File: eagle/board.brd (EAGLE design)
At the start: 75 x 50 mm, 24 parts, among them X1 2.1MMJACKTHM, X10 10p-2.0, X11 MOUNTING_HOLE3.2MM_SILK, X12 MOUNTING_HOLE3.2MM_SILK, X13 MOUNTING_HOLE3.2MM_SILK, X14 MOUNTING_HOLE3.2MM_SILK, X2 2p-2.0, X3 5p-2.54, X4 8p-2.54, X5 14p-2.54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

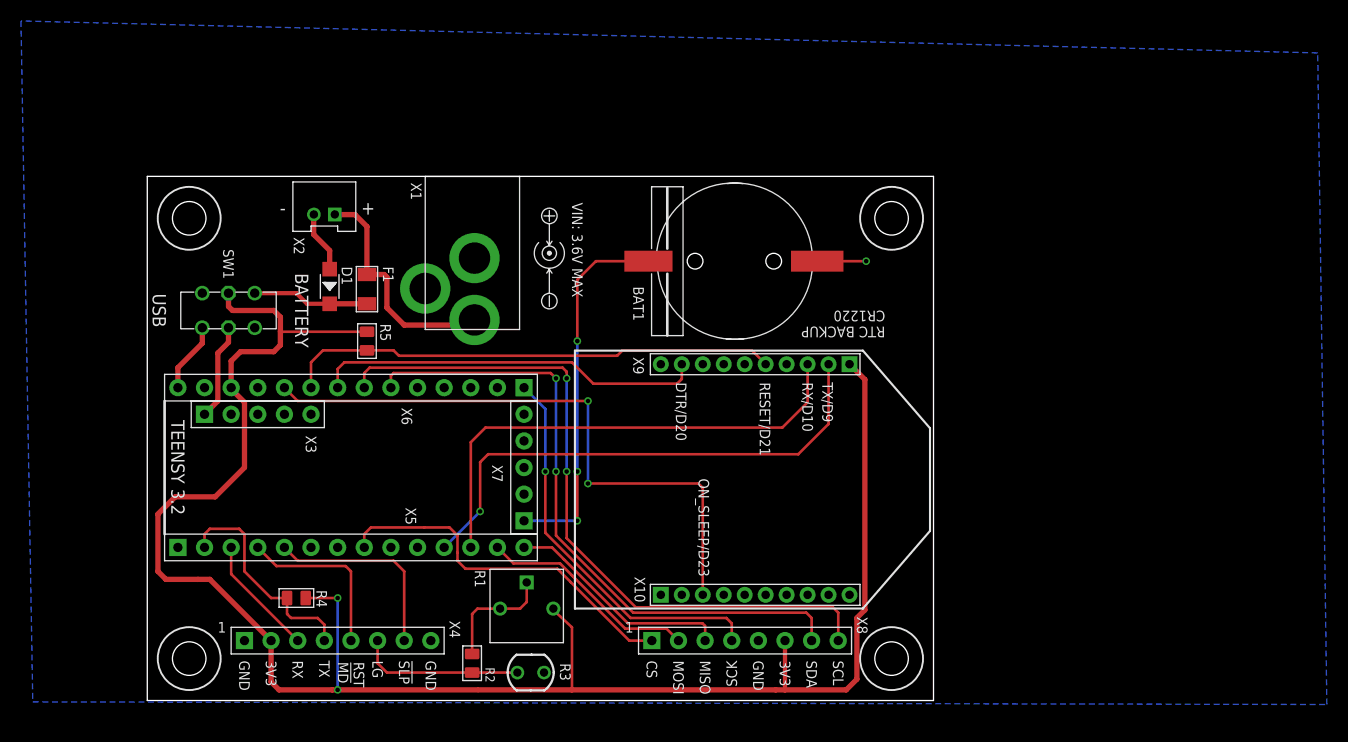
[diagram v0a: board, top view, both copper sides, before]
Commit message: new slide switch new capacitors
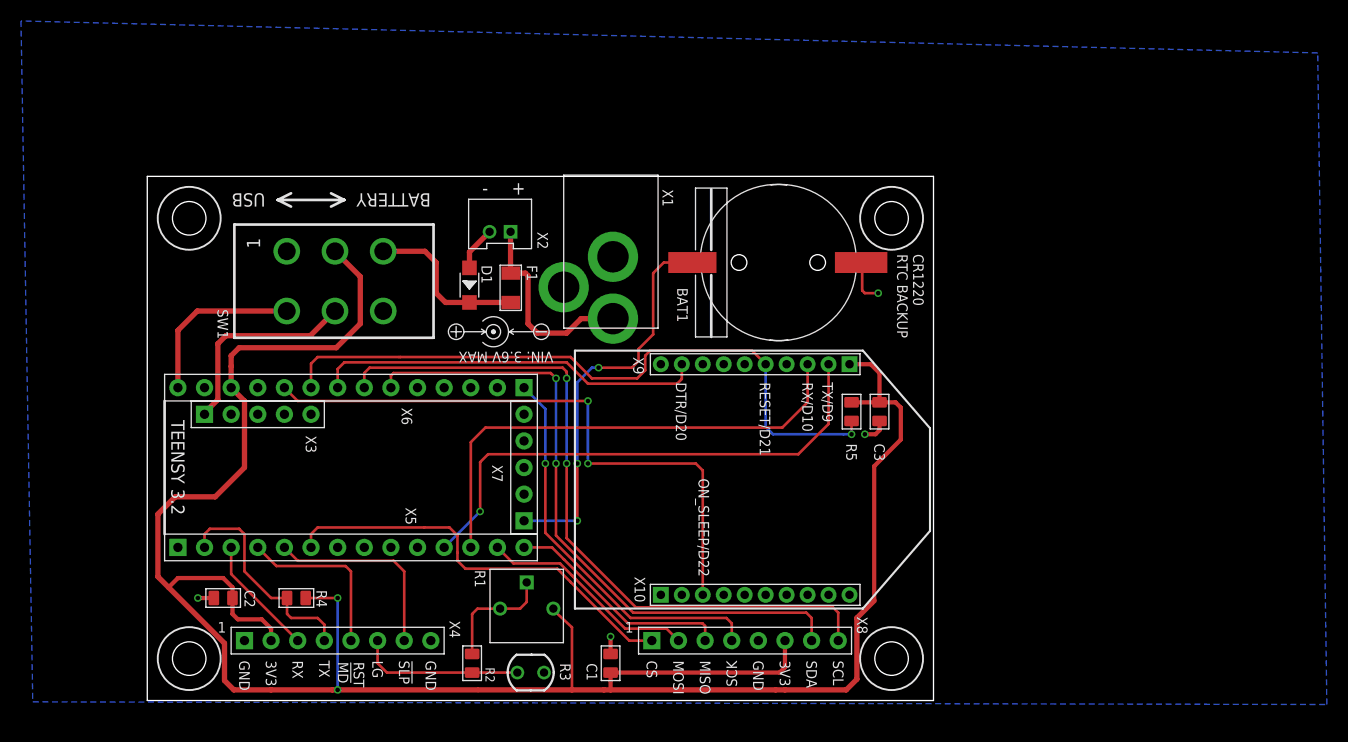
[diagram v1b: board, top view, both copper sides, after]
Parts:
- added C1, C2, C3: 2.2uf, Seeed-OPL-Capacitor:C0805
- SW1: value (none) -> C&K L202XXYYXMS; device teensybee:SW6-2.54-9.0X3.5X3.2+2.0MM -> teensybee:C&K_L102_MS
- moved R5 46.7 mm to (67.2, 27.6)
- moved X2 16.8 mm to (33.7, 45.5)
- moved F1 13.7 mm to (34.7, 39.4)
- moved D1 13.3 mm to (30.7, 39.6)
- moved X1 13.2 mm to (44.3, 45.7)
- moved SW1 10.5 mm to (17.9, 40.0), turned to 270 degrees
- moved U$1 9.20 mm to (33.0, 35.2), turned to 0 degrees
- moved BAT1 4.19 mm to (60.2, 41.8)
- renumbered X11 to MNT1, X12 to MNT2, X13 to MNT3, X14 to MNT4
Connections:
- net +3V3: now also C1.2, C2.2, C3.1, SW1.2; no longer SW1.COM2
- net GND: now also C1.1, C2.1, C3.2
- net N$13: now also X5.6; no longer X5.8
- net N$18: now also SW1.4; no longer SW1.CH1A
- net N$19: now also SW1.5; no longer SW1.COM1
- net N$20: now also SW1.3; no longer SW1.CH2B
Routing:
- net +3V3: track 179.2 -> 217.1 mm
- net N$16: track 47.2 -> 65.0 mm, vias 0 -> 1
- net N$19: track 9.20 -> 19.7 mm
- net N$18: track 6.68 -> 16.6 mm
- net N$13: track 34.8 -> 39.9 mm
- net N$20: track 11.1 -> 15.9 mm
- net GND: track 10.5 -> 14.2 mm, vias 1 -> 4
- net N$23: track 22.2 -> 19.3 mm
- net N$3: track 35.6 -> 38.1 mm
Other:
- board text added: "CR1220 RTC BACKUP"
- board text added: "ON_SLEEP/D22"
- board text removed: "ON_SLEEP/D23"
- board text removed: "RTC BACKUP CR1220"
